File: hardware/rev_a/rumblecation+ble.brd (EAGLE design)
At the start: 73.6 x 36.3 mm, 76 parts, among them J1 FCI_CORTEX_SWD_CONNECTOR, J2 JST_S2B-PH-SM4-TB_CONNECTOR, J3 MINI_USB_B, J6 TC2030-JLINK-NL, M1 PRECISION_MICRODRIVES_C100-10, M2 PRECISION_MICRODRIVES_310-113, U1 ATSAMD4S2BA-AU, U2 SILABS_CP2102, U3 TLV73333PDBVT, U4 TI_DRV2603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

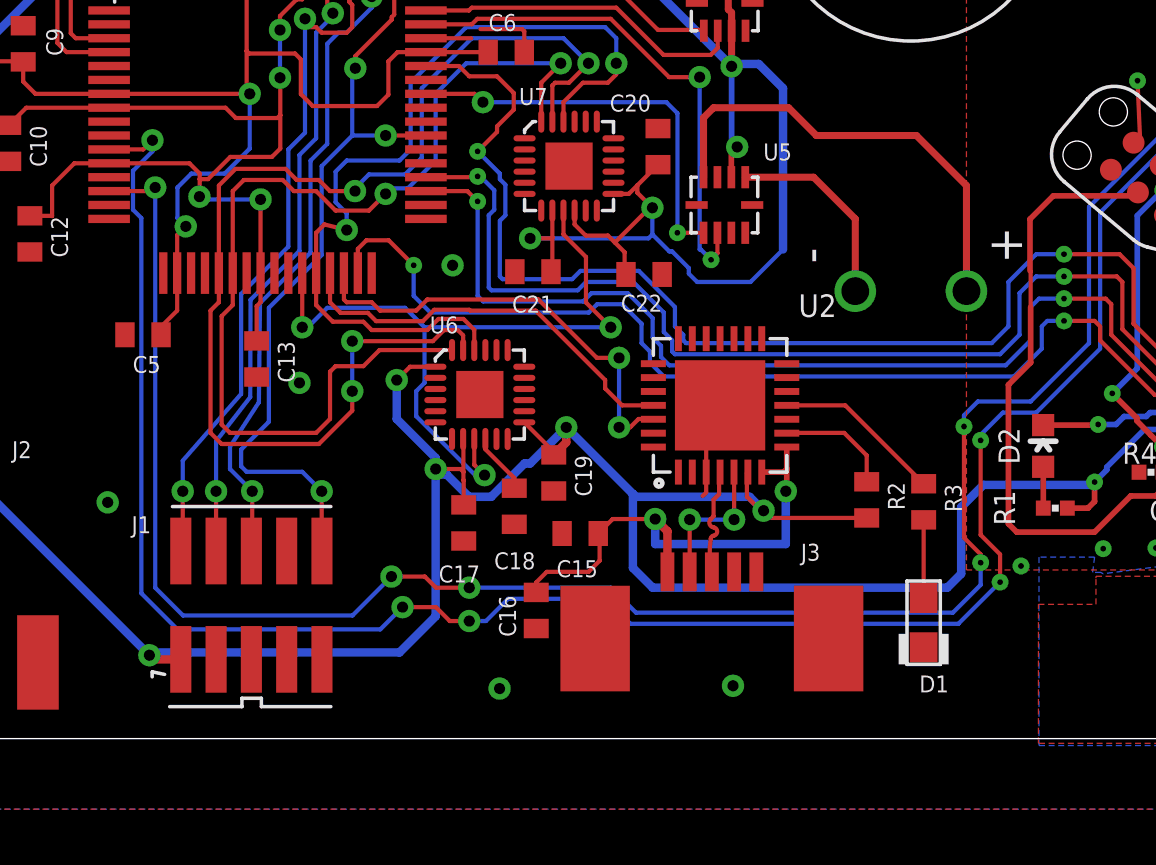
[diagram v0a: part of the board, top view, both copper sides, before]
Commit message: fixed silab usb-uart, added fsync and int to accell, updated schematic prettiness, fixed regout on accel
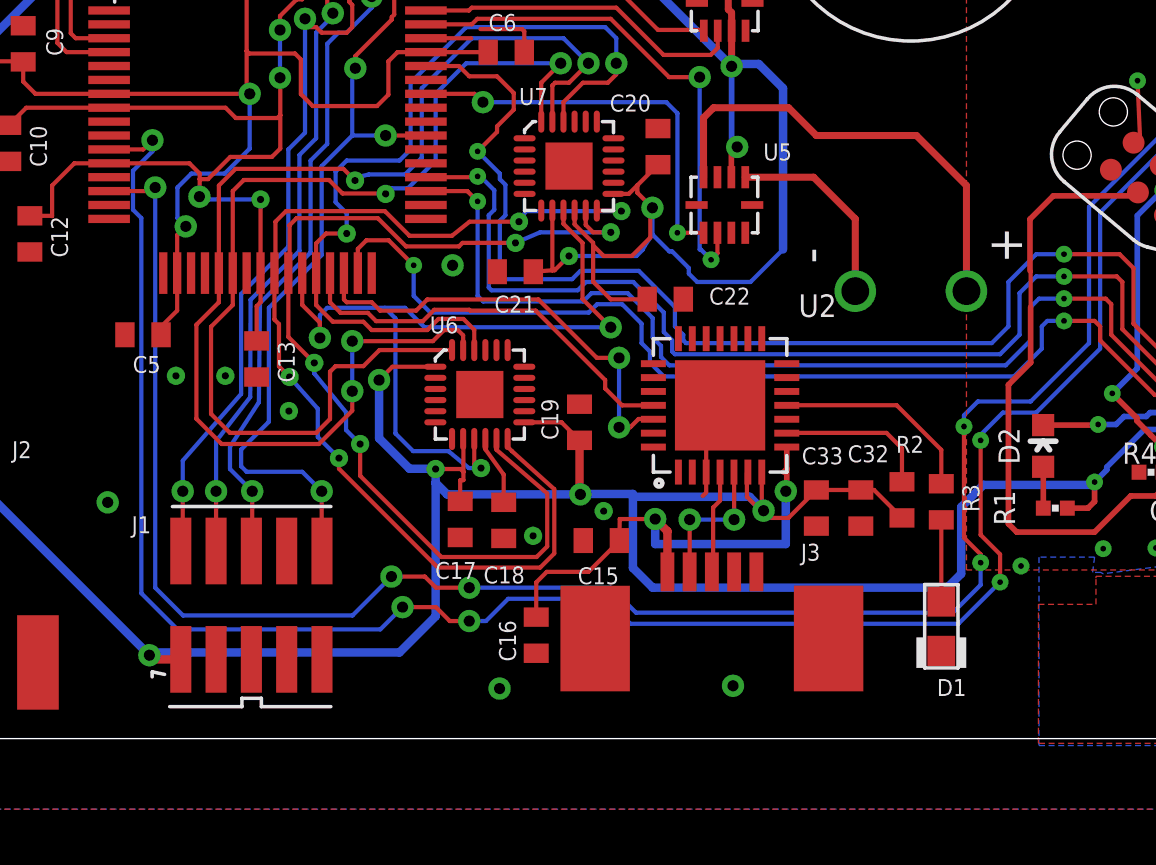
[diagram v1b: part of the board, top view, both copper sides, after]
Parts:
- added C32: 4.7uF, rumbleaction_parts_lib:C0402
- added C33: 100nF, rumbleaction_parts_lib:C0402
- U1: value ATSAMD4S2BA-AU -> ATSAM4S2BA-AU
- moved C19 2.04 mm to (28.5, 11.5), turned to 90 degrees
- moved R2 1.27 mm to (40.1, 8.66)
- moved C22 1.17 mm to (31.6, 15.9)
- moved C16 0.89 mm to (26.9, 3.79)
- moved C15 0.80 mm to (29.3, 7.20)
- moved D1 0.65 mm to (41.5, 4.11)
- moved C18 0.64 mm to (25.7, 7.92)
- moved C21 0.63 mm to (26.2, 16.9)
- moved R3 0.63 mm to (41.5, 8.59)
- moved C17 0.18 mm to (24.2, 7.96)
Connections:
- net D+ renamed USB_D_P
- net D- renamed USB_D_N
- net N$4 renamed USB_LED
- new net MPU_FSYNC: U1.P$26, U6.P$11, U7.P$11
- new net MPU_INT: U1.P$25, U6.P$12, U7.P$12
- net +3V3: now also C32.1, C33.1, U2.P$7
- net GND: now also C32.2, C33.2
- net VBUS: no longer U2.P$7
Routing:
- net MPU_INT: track 0.00 -> 38.4 mm, vias 0 -> 4
- net MPU_FSYNC: track 0.00 -> 36.6 mm, vias 0 -> 4
- net +3V3: track 258.5 -> 265.6 mm
- net MPU_MISO: track 26.6 -> 28.6 mm
- net N$1: track 4.16 -> 5.58 mm
- net USB_LED: track 6.09 -> 7.45 mm
- net GND: vias 36 -> 40

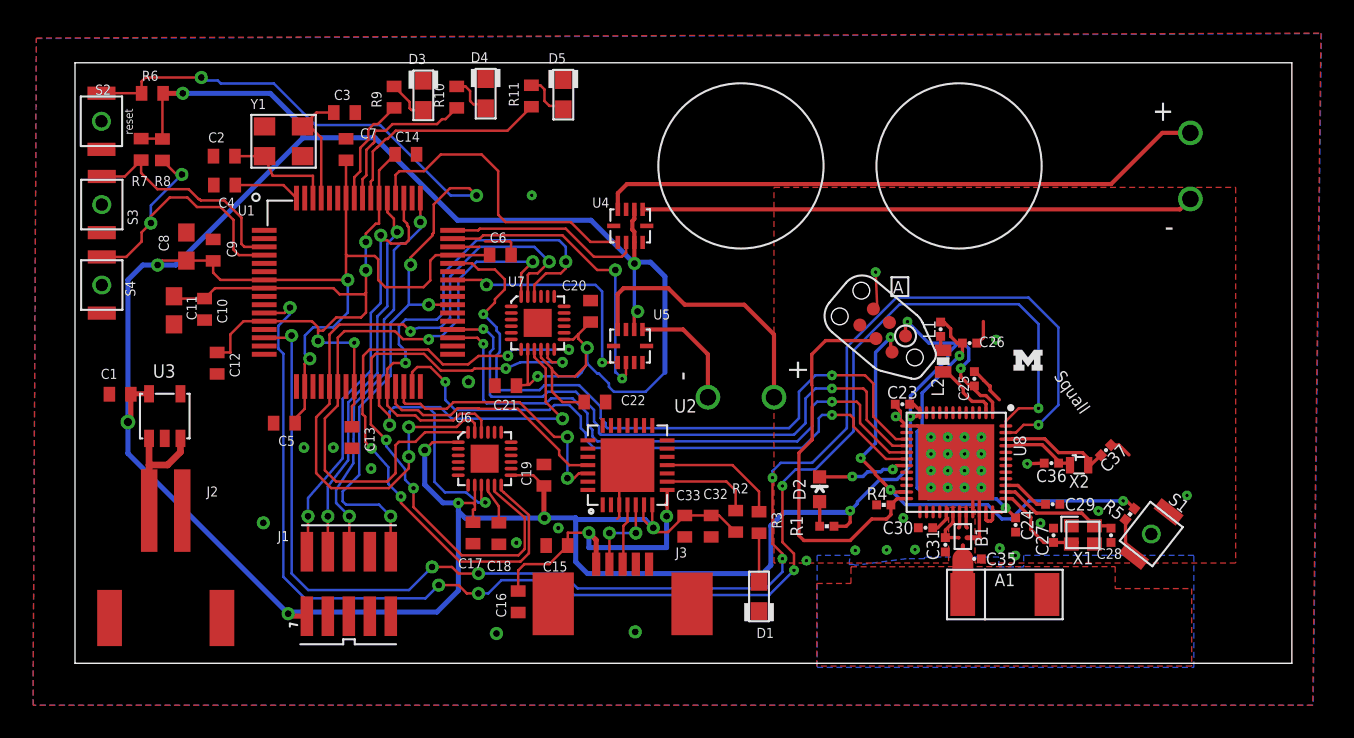
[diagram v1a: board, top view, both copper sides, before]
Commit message: Added a power selector header, fixed some routing errors
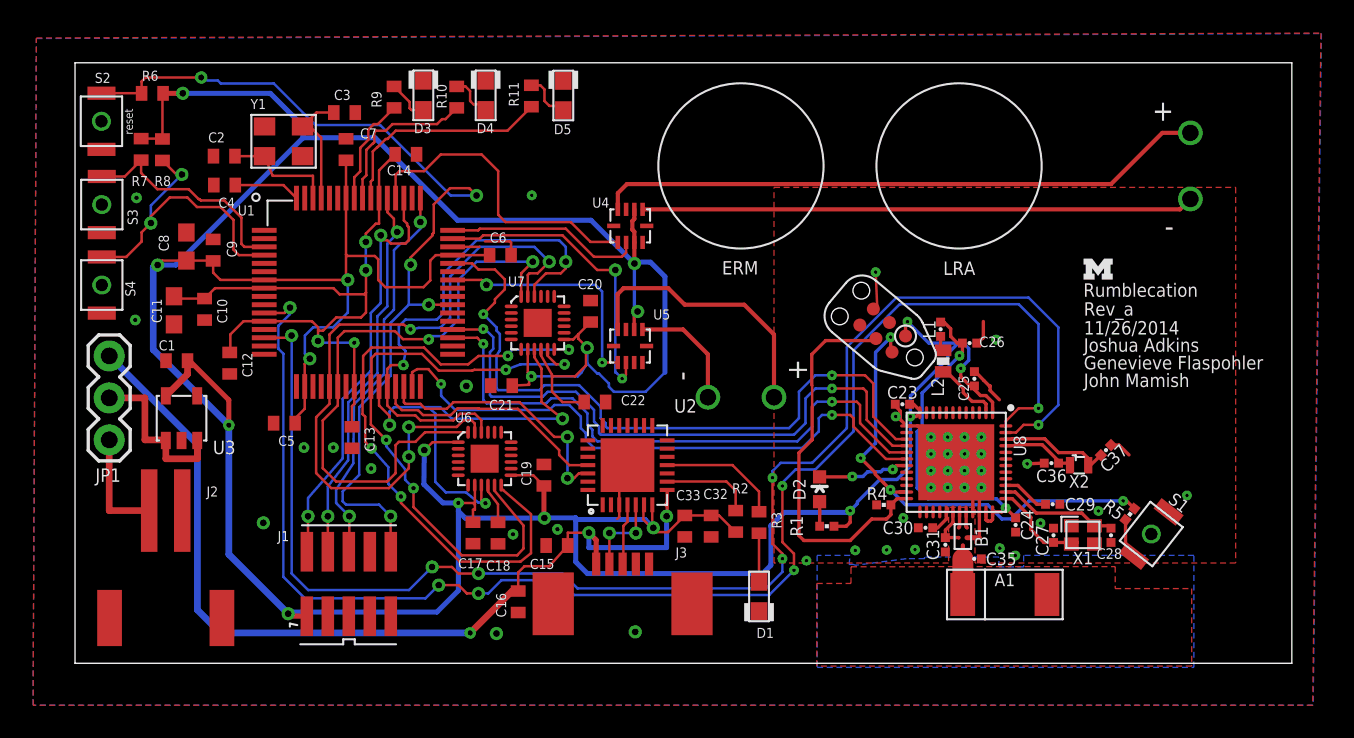
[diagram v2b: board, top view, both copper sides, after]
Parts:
- added JP1: (no value), SparkFun-Connectors:1X03
- moved LOGO1 6.96 mm to (62.0, 23.9)
- moved C1 3.99 mm to (6.25, 18.4)
- moved U3 1.02 mm to (5.59, 16.3)
- moved C12 0.76 mm to (9.45, 18.2)
- moved C21 0.25 mm to (25.9, 16.9)
- moved D4 0.10 mm to (24.9, 34.4)
- moved C18 0.06 mm to (25.7, 7.95)
- moved D5 0.05 mm to (29.6, 34.4)
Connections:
- new net N$4: JP1.2, U3.P$1, U3.P$3
- net N$7: now also JP1.1; no longer U3.P$1, U3.P$3
- net VBUS: now also JP1.3
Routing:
- net VBUS: track 18.3 -> 56.9 mm, vias 2 -> 3
- net N$4: track 0.00 -> 10.1 mm
- net +3V3: track 265.6 -> 268.7 mm
- net N$7: track 7.82 -> 6.70 mm
- net VDDOUT: track 41.9 -> 41.1 mm
- net GND: vias 40 -> 42
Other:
- board text added: "11/26/2014"
- board text added: "ERM"
- board text added: "Genevieve Flaspohler"
- board text added: "John Mamish"
- board text added: "Joshua Adkins"
- board text added: "LRA"
- board text added: "Rev_a"
- board text added: "Rumblecation"
- board text removed: "2014/10/08"
- board text removed: "A"
- board text removed: "Brad Campbell"
- board text removed: "Squall"

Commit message: Final board revision - being sent for production
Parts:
- moved LOGO1 3.12 mm to (59.0, 24.6)
